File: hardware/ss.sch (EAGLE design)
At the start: 76 parts, among them IC1 DS3231, Q1 BSS138, Q3 si2305cd, Q4 si2305cd, Q5 8MHz, Q6 si2305cd, U1 SPX5205 3v3, U17 AVR_SPI_PRG_6PTH, U2 CN3083, U3 SPX5205 3v3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

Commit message: latest
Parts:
- removed BAT1: 3v, SparkFun:BATTERY12MM
- removed Q3: si2305cd, Simplex-DiscreteSemi:MOSFET-PCHANNELSMD_POWER
- added C22: 100nF, rcl:C-EUC0805
- added JP11: analog, SparkFun:M06SIP
- added JP14: digital, SparkFun-Connectors:M07
- added JP8: JUMPER-3SMD, SparkFun-Passives:JUMPER-3SMD
- added JP9: Kterm, SparkFun:M02PTH
- added Q2: si2305cd, Simplex-DiscreteSemi:MOSFET-PCHANNELSMD_POWER
- added R16: 100k, rcl:R-EU_R0805W
- added SJ3, SJ4: SOLDERJUMPERTRACE, SparkFun-Passives:SOLDERJUMPERTRACE
- added T1: BC846, transistor:BC846
- added U$3: MAX6675, SparkFun-AnalogIC:MAX6675
- JP4: value uC -> M01PTH; device SparkFun:M02PTH -> SparkFun-Connectors:M01PTH
- JP5: value digital -> 3v Li bat; device SparkFun-Connectors:M081X08 -> SparkFun:M02PTH
- JP6: value analog -> rxtx; device SparkFun-Connectors:M06SIP -> SparkFun:M02PTH
- LED1: value red -> charging; device SparkFun:LED0603 -> led:LEDCHIP-LED0805
- LED2: value green -> full; device SparkFun:LED0603 -> led:LEDCHIP-LED0805
- LED4: device SparkFun:LED0603 -> led:LEDCHIP-LED0805
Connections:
- removed net D4: JP5.2, U5.PD4(XCK/T0)
- removed net N$4: IC1.SDA, JP4.2, R13.2
- removed net N$6: IC1.SCL, JP4.1, R10.2
- removed net XBEE_IN: C18.1, C20.1, Q3.D, U3.EN, U3.IN
- removed net XBEE_PWR_SW: Q3.G, R1.2, U$2.DTR, U5.PC2(ADC2)
- new net A2: JP8.2, JP8.3, U5.PC2(ADC2)
- new net A3: JP11.4, U5.PC3(ADC3)
- new net N$100: C16.1, C17.1, Q2.S, R1.2, SJ3.2, U3.OUT
- new net N$26: R7.1, T1.B
- new net N$27: Q4.G, R16.2, T1.C
- new net N$29: JP9.1, U$3.T+
- new net N$30: JP9.2, U$3.T-
- new net XBEE_HIB: SJ4.1, U$2.DTR
- new net XBEE_PWR_SW_M: JP8.1, Q2.G, R1.1
- net +3V3: now also C22.1, U$3.VDD
- net +3V3_XBEE: now also Q2.D, SJ3.1; no longer C16.1, C17.1, U3.OUT
- net A0: now also JP11.2; no longer JP6.1
- net A1: now also JP11.3; no longer JP6.2
- net A6: now also JP4.1; no longer JP6.5
- net A7: now also JP11.1; no longer JP6.6
- net BOOST_SW: now also U5.PD4(XCK/T0); no longer Q4.G, U5.PC3(ADC3)
- net D3: now also JP14.2; no longer JP5.1
- net D5: now also JP14.3; no longer JP5.3
- net D6: now also JP14.4; no longer JP5.4
- net D7: now also JP14.5; no longer JP5.5
- net D8: now also JP14.6; no longer JP5.6
- net D9: now also JP14.7, U$3.CS; no longer JP5.7
- net GND: now also C22.2, JP5.2, SJ4.2, T1.E, U$3.VSS; no longer BAT1.-
- net H1: now also JP14.1; no longer JP5.8
- net MISO: now also U$3.MISO
- net N$10: now also JP5.1; no longer BAT1.+
- net RXI: now also JP6.1
- net SCK: now also U$3.SCK
- net SCL: now also IC1.SCL, JP11.6, R10.2; no longer JP6.4
- net SDA: now also IC1.SDA, JP11.5, R13.2; no longer JP6.3
- net TXO: now also JP6.2
- net V+: no longer Q3.S, Q4.S, R1.1, R7.1
- net VIN: now also C18.1, C20.1, Q4.S, R16.1, U3.EN, U3.IN
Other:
- moved on the sheet: C16, C17, C18, C19, C20, LED1, LED2, LED4, Q4, R1, R7, U3

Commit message: latest
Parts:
- removed JP8: JUMPER-3SMD, SparkFun-Passives:JUMPER-3SMD
- removed SJ3, SJ4: SOLDERJUMPERTRACE, SparkFun-Passives:SOLDERJUMPERTRACE
- added JP10: power, SparkFun:M02PTH
- added SJ345: J345, Simplex-Jumpers:SJ_4P
- added SJ6: J6, jumper:SJ
- JP4: value M01PTH -> a6
- SJ1: value SOLDERJUMPERTRACE -> J1; device SparkFun-Passives:SOLDERJUMPERTRACE -> jumper:SJ
- SJ2: value SOLDERJUMPERTRACE -> J2; device SparkFun-Passives:SOLDERJUMPERTRACE -> jumper:SJ
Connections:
- removed net A2: JP8.2, JP8.3, U5.PC2(ADC2)
- removed net N$100: C16.1, C17.1, Q2.S, R1.2, SJ3.2, U3.OUT
- removed net N$18: SJ2.2, U$2.RSSI
- removed net N$20: R8.2, SJ2.1
- new net N$7: R8.2, SJ6.1, SJ6.2, U$2.RSSI
- net +3V3_XBEE: now also C16.1, C17.1, Q2.S, R1.2, SJ2.1, SJ2.2, U3.OUT; no longer SJ3.1
- net GND: now also JP10.1, SJ345.4; no longer SJ4.2
- net N$12: now also JP10.2
- net XBEE_HIB: now also SJ345.2, SJ345.3, U5.PC2(ADC2); no longer SJ4.1
- net XBEE_PWR_SW_M: now also SJ345.1; no longer JP8.1
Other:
- note added: "J1 set - enable RST after schetch upload via xbee (default OPEN)"
- note added: "J2 set - xbee always has power on Vdd (default SET)"
- note added: "J3 set - xbee power controlled by external mosfet (default OPEN)"
- note added: "J4 set - xbee power controlled by ATSM1 (pin wake mode) (default SET)"
- note added: "J5 set - xbee always up if ATSM1 (pin wake mode) is used (default OPEN)"
- note added: "J6 set - xbee RSSI (Receive Signal Strength Indicator) displayed via an LED (default SET)"
- note added: "solder jumper settings"
- note added: "some combinations of J2,3,4,5 can fry devices. think twice."
- moved on the sheet: JP11, JP4

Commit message: latest
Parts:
- removed X1: USBSMD, SparkFun-Connectors:USBSMD
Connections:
- removed net N$23: LED4.A, R8.1
- new net N$6: LED4.C, R8.2
- net GND: now also R8.1, SJ6.1, SJ6.2; no longer LED4.C, X1.GND
- net N$12: no longer X1.VBUS
- net N$7: now also LED4.A; no longer R8.2, SJ6.1, SJ6.2
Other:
- moved on the sheet: JP10, JP2, LED4, SJ6
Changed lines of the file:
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@@
 <part name="GND7" library="SparkFun" deviceset="GND" device=""/>
 <part name="GND8" library="SparkFun" deviceset="GND" device=""/>
-<part name="GND12" library="SparkFun" deviceset="GND" device=""/>
 <part name="R5" library="rcl" deviceset="R-EU_" device="R0805W" value="1K"/>
 <part name="C5" library="rcl" deviceset="C-EU" device="C1206" value="10uF"/>
@@
 <part name="C20" library="rcl" deviceset="C-EU" device="C0805" value="100nF"/>
 <part name="GND32" library="SparkFun" deviceset="GND" device=""/>
-<part name="X1" library="SparkFun-Connectors" deviceset="USB" device="SMD"/>
 <part name="C15" library="rcl" deviceset="C-EU" device="C0805" value="100nF"/>
 <part name="Q4" library="Simplex-DiscreteSemi" deviceset="MOSFET-PCHANNEL" device="SMD_POWER" value="si2305cd"/>
@@
 <instance part="GND7" gate="1" x="33.02" y="149.86"/>
 <instance part="GND8" gate="1" x="48.26" y="149.86"/>
-<instance part="GND12" gate="1" x="15.24" y="149.86"/>
 <instance part="R5" gate="G$1" x="35.56" y="182.88" rot="R180"/>
 <instance part="C5" gate="G$1" x="78.74" y="160.02"/>
@@
 <instance part="IC1" gate="G$1" x="182.88" y="25.4"/>
 <instance part="GND21" gate="1" x="165.1" y="5.08"/>
-<instance part="JP2" gate="G$1" x="17.78" y="121.92" rot="R90"/>
+<instance part="JP2" gate="G$1" x="7.62" y="132.08"/>
 <instance part="+3V1" gate="G$1" x="86.36" y="139.7"/>
 <instance part="+3V2" gate="G$1" x="152.4" y="43.18"/>
@@
 <instance part="+3V6" gate="G$1" x="228.6" y="55.88"/>
 <instance part="P+4" gate="1" x="88.9" y="175.26"/>
-<instance part="P+5" gate="1" x="15.24" y="139.7"/>
+<instance part="P+5" gate="1" x="20.32" y="139.7"/>
 <instance part="P+6" gate="1" x="132.08" y="43.18"/>
 <instance part="P+9" gate="1" x="10.16" y="38.1"/>
@@
 <instance part="C20" gate="G$1" x="15.24" y="86.36"/>
 <instance part="GND32" gate="1" x="15.24" y="76.2"/>
-<instance part="X1" gate="G$1" x="10.16" y="162.56" rot="MR0"/>
 <instance part="C15" gate="G$1" x="20.32" y="160.02"/>
 <instance part="Q4" gate="G$1" x="10.16" y="60.96" rot="MR180"/>
@@
 <instance part="GND43" gate="1" x="203.2" y="190.5"/>
 <instance part="JP9" gate="G$1" x="205.74" y="210.82" rot="R180"/>
-<instance part="LED4" gate="G$1" x="254" y="167.64" rot="MR90"/>
+<instance part="LED4" gate="G$1" x="274.32" y="167.64" rot="MR90"/>
 <instance part="JP5" gate="G$1" x="223.52" y="20.32" rot="R180"/>
 <instance part="LED2" gate="G$1" x="55.88" y="187.96" rot="MR270"/>
@@
 <instance part="JP4" gate="G$1" x="287.02" y="91.44" rot="R180"/>
 <instance part="JP14" gate="G$1" x="304.8" y="83.82" rot="R180"/>
-<instance part="JP10" gate="G$1" x="7.62" y="177.8"/>
-<instance part="GND46" gate="1" x="15.24" y="172.72"/>
+<instance part="JP10" gate="G$1" x="7.62" y="162.56"/>
+<instance part="GND46" gate="1" x="15.24" y="149.86"/>
 <instance part="SJ1" gate="1" x="325.12" y="172.72"/>
-<instance part="SJ6" gate="1" x="274.32" y="167.64"/>
+<instance part="SJ6" gate="1" x="254" y="167.64"/>
 <instance part="SJ2" gate="1" x="93.98" y="88.9" rot="R90"/>
 <instance part="SJ345" gate="G$1" x="241.3" y="129.54"/>
@@
 </segment>
 <segment>
-<wire x1="12.7" y1="162.56" x2="15.24" y2="162.56" width="0.1524" layer="91"/>
-<wire x1="15.24" y1="162.56" x2="15.24" y2="152.4" width="0.1524" layer="91"/>
-<pinref part="GND12" gate="1" pin="GND"/>
-<pinref part="X1" gate="G$1" pin="GND"/>
-</segment>
-<segment>
 <wire x1="35.56" y1="170.18" x2="33.02" y2="170.18" width="0.1524" layer="91"/>
 <wire x1="33.02" y1="170.18" x2="33.02" y2="152.4" width="0.1524" layer="91"/>
@@
 </segment>
 <segment>
-<pinref part="GND34" gate="1" pin="GND"/>
-<wire x1="248.92" y1="162.56" x2="248.92" y2="167.64" width="0.1524" layer="91"/>
-<pinref part="LED4" gate="G$1" pin="C"/>
-</segment>
-<segment>
 <pinref part="T1" gate="G$1" pin="E"/>
 <pinref part="GND33" gate="1" pin="GND"/>
@@
 <pinref part="JP10" gate="G$1" pin="1"/>
 <pinref part="GND46" gate="1" pin="GND"/>
-<wire x1="15.24" y1="177.8" x2="15.24" y2="175.26" width="0.1524" layer="91"/>
+<wire x1="15.24" y1="162.56" x2="15.24" y2="152.4" width="0.1524" layer="91"/>
 </segment>
 <segment>
@@
 <wire x1="228.6" y1="129.54" x2="236.22" y2="129.54" width="0.1524" layer="91"/>
 </segment>
+<segment>
+<pinref part="GND34" gate="1" pin="GND"/>
+<pinref part="SJ6" gate="1" pin="1"/>
+<wire x1="248.92" y1="162.56" x2="248.92" y2="167.64" width="0.1524" layer="91"/>
+<wire x1="248.92" y1="167.64" x2="248.92" y2="172.72" width="0.1524" layer="91"/>
+<wire x1="248.92" y1="172.72" x2="259.08" y2="172.72" width="0.1524" layer="91"/>
+<pinref part="R8" gate="G$1" pin="1"/>
+<pinref part="SJ6" gate="1" pin="2"/>
+<wire x1="259.08" y1="172.72" x2="259.08" y2="167.64" width="0.1524" layer="91"/>
+<junction x="248.92" y="167.64"/>
+<junction x="259.08" y="167.64"/>
+</segment>
 </net>
 <net name="VIN" class="0">
@@
 <wire x1="40.64" y1="132.08" x2="40.64" y2="121.92" width="0.1524" layer="91"/>
 <wire x1="40.64" y1="121.92" x2="50.8" y2="121.92" width="0.1524" layer="91"/>
-<wire x1="17.78" y1="129.54" x2="17.78" y2="132.08" width="0.1524" layer="91"/>
-<wire x1="17.78" y1="132.08" x2="27.94" y2="132.08" width="0.1524" layer="91"/>
+<wire x1="15.24" y1="132.08" x2="27.94" y2="132.08" width="0.1524" layer="91"/>
 <wire x1="27.94" y1="132.08" x2="35.56" y2="132.08" width="0.1524" layer="91"/>
 <wire x1="35.56" y1="132.08" x2="40.64" y2="132.08" width="0.1524" layer="91"/>
@@
 <wire x1="30.48" y1="182.88" x2="27.94" y2="182.88" width="0.1524" layer="91"/>
 <wire x1="27.94" y1="182.88" x2="27.94" y2="165.1" width="0.1524" layer="91"/>
-<wire x1="12.7" y1="165.1" x2="20.32" y2="165.1" width="0.1524" layer="91"/>
 <wire x1="20.32" y1="165.1" x2="27.94" y2="165.1" width="0.1524" layer="91"/>
 <wire x1="27.94" y1="165.1" x2="27.94" y2="162.56" width="0.1524" layer="91"/>
@@
 <pinref part="R5" gate="G$1" pin="2"/>
 <pinref part="C14" gate="G$1" pin="+"/>
-<pinref part="X1" gate="G$1" pin="VBUS"/>
 <pinref part="C15" gate="G$1" pin="1"/>
 <pinref part="JP10" gate="G$1" pin="2"/>
-<wire x1="15.24" y1="180.34" x2="20.32" y2="180.34" width="0.1524" layer="91"/>
-<wire x1="20.32" y1="180.34" x2="20.32" y2="165.1" width="0.1524" layer="91"/>
+<wire x1="15.24" y1="165.1" x2="20.32" y2="165.1" width="0.1524" layer="91"/>
 </segment>
 </net>
@@
 </segment>
 <segment>
-<wire x1="15.24" y1="137.16" x2="15.24" y2="129.54" width="0.1524" layer="91"/>
-<pinref part="P+5" gate="1" pin="V+"/>
-<pinref part="JP2" gate="G$1" pin="2"/>
-</segment>
-<segment>
 <wire x1="132.08" y1="40.64" x2="132.08" y2="30.48" width="0.1524" layer="91"/>
 <wire x1="132.08" y1="30.48" x2="134.62" y2="30.48" width="0.1524" layer="91"/>
@@
 <pinref part="R11" gate="G$1" pin="2"/>
 <pinref part="Q6" gate="G$1" pin="S"/>
+</segment>
+<segment>
+<pinref part="JP2" gate="G$1" pin="2"/>
+<pinref part="P+5" gate="1" pin="V+"/>
+<wire x1="15.24" y1="134.62" x2="20.32" y2="134.62" width="0.1524" layer="91"/>
+<wire x1="20.32" y1="134.62" x2="20.32" y2="137.16" width="0.1524" layer="91"/>
 </segment>
 </net>
@@
 </segment>
 </net>
-<net name="N$23" class="0">
-<segment>
-<pinref part="R8" gate="G$1" pin="1"/>
-<pinref part="LED4" gate="G$1" pin="A"/>
-<wire x1="256.54" y1="167.64" x2="259.08" y2="167.64" width="0.1524" layer="91"/>
-</segment>
-</net>
 <net name="A6" class="0">
 <segment>
@@
 </segment>
 </net>
+<net name="N$6" class="0">
+<segment>
+<pinref part="R8" gate="G$1" pin="2"/>
+<pinref part="LED4" gate="G$1" pin="C"/>
+</segment>
+</net>
 <net name="N$7" class="0">
 <segment>
-<pinref part="R8" gate="G$1" pin="2"/>
-<pinref part="SJ6" gate="1" pin="1"/>
-<wire x1="269.24" y1="167.64" x2="269.24" y2="170.18" width="0.1524" layer="91"/>
-<wire x1="269.24" y1="170.18" x2="276.86" y2="170.18" width="0.1524" layer="91"/>
-<wire x1="276.86" y1="170.18" x2="276.86" y2="167.64" width="0.1524" layer="91"/>
+<pinref part="LED4" gate="G$1" pin="A"/>
 <pinref part="U$2" gate="G$1" pin="RSSI"/>
-<pinref part="SJ6" gate="1" pin="2"/>
 <wire x1="276.86" y1="167.64" x2="279.4" y2="167.64" width="0.1524" layer="91"/>
-<junction x="269.24" y="167.64"/>
-<junction x="279.4" y="167.64"/>
-</segment>
-</net>
+</segment>
+</net>

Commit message: hopefully flawless
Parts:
- removed Q2: si2305cd, Simplex-DiscreteSemi:MOSFET-PCHANNELSMD_POWER
- removed R1: 100k, rcl:R-EU_R0805W
- added Q3: si2305cd, Simplex-DiscreteSemi:MOSFET-PCHANNELSMD_POWER
- added R17: 1M, rcl:R-EU_R0805W
- added R18: 100k, rcl:R-EU_R0805W
- added T2: BC846, transistor:BC846
- R7: value 100k -> 1M
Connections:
- new net N$18: R17.1, T2.B
- new net N$20: Q3.G, R18.2, T2.C
- net +3V3_XBEE: no longer Q2.D, Q2.S, R1.2, SJ2.1, SJ2.2
- net GND: now also T2.E
- net VIN: now also Q3.D, Q3.S, R18.1, SJ2.1, SJ2.2
- net XBEE_PWR_SW_M: now also R17.2; no longer Q2.G, R1.1
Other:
- moved on the sheet: C1, C14, C15, C16, C17, C18, C19, C2, C20, C3, C4, C5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

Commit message: d9 needs external weak pullup during programming
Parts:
- added R1: 100K, rcl:R-EU_R0805W
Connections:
- net +3V3: now also R1.2
- net D9: now also R1.1
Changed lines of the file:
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@@
 <part name="R18" library="rcl" deviceset="R-EU_" device="R0805W" value="100k"/>
 <part name="SJ2" library="jumper" deviceset="SJ" device="" value="J2"/>
+<part name="+3V9" library="supply1" deviceset="+3V3" device=""/>
+<part name="R1" library="rcl" deviceset="R-EU_" device="R0805W" value="100K"/>
 </parts>
 <sheets>
@@
 <instance part="R18" gate="G$1" x="0" y="129.54" rot="R270"/>
 <instance part="SJ2" gate="1" x="30.48" y="127" rot="R90"/>
+<instance part="+3V9" gate="G$1" x="233.68" y="99.06"/>
+<instance part="R1" gate="G$1" x="223.52" y="91.44"/>
 </instances>
 <busses>
@@
 <junction x="149.86" y="210.82"/>
 </segment>
+<segment>
+<pinref part="+3V9" gate="G$1" pin="+3V3"/>
+<wire x1="233.68" y1="91.44" x2="233.68" y2="96.52" width="0.1524" layer="91"/>
+<pinref part="R1" gate="G$1" pin="2"/>
+<wire x1="228.6" y1="91.44" x2="233.68" y2="91.44" width="0.1524" layer="91"/>
+</segment>
 </net>
 <net name="+5V" class="0">
@@
 <segment>
 <pinref part="U5" gate="G$1" pin="PD4(XCK/T0)"/>
+<label x="210.82" y="106.68" size="1.778" layer="95"/>
 <wire x1="208.28" y1="106.68" x2="215.9" y2="106.68" width="0.1524" layer="91"/>
-<label x="210.82" y="106.68" size="1.778" layer="95"/>
 </segment>
 </net>
@@
 <segment>
 <pinref part="U5" gate="G$1" pin="PB1(OC1A)"/>
-<wire x1="208.28" y1="91.44" x2="215.9" y2="91.44" width="0.1524" layer="91"/>
+<wire x1="208.28" y1="91.44" x2="218.44" y2="91.44" width="0.1524" layer="91"/>
 <label x="210.82" y="91.44" size="1.778" layer="95"/>
-</segment>
-<segment>
+<pinref part="R1" gate="G$1" pin="1"/>
+</segment>
+<segment>

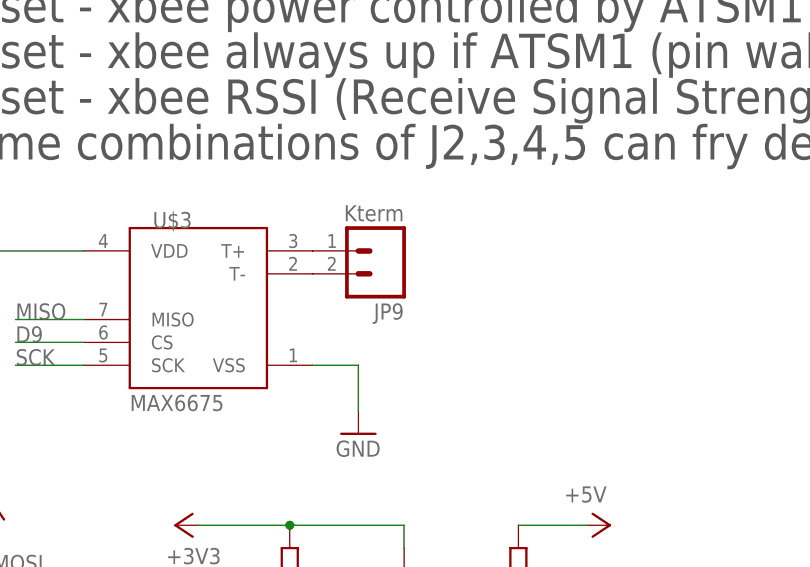
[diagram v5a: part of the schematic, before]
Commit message: thermocouple t- must be grounded
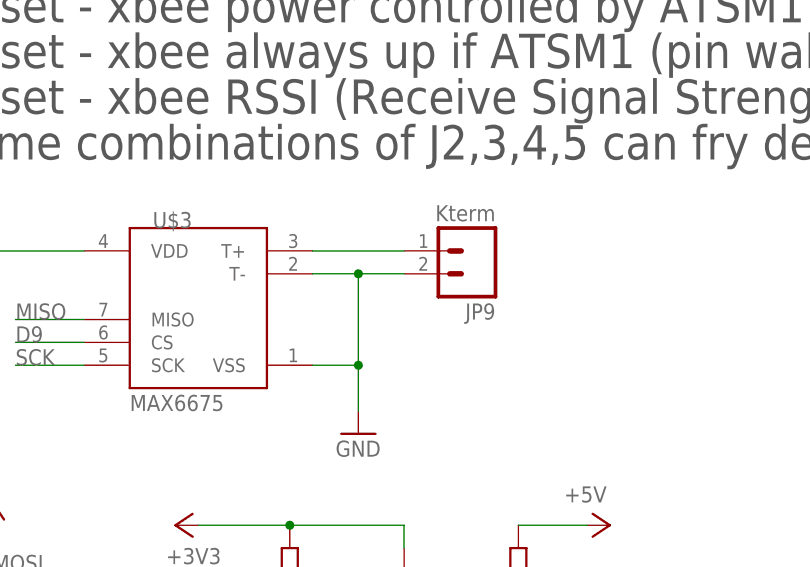
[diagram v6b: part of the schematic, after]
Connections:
- removed net N$30: JP9.2, U$3.T-
- net GND: now also JP9.2, U$3.T-
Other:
- moved on the sheet: JP9
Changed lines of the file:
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@@
 <instance part="GND37" gate="1" x="149.86" y="190.5"/>
 <instance part="GND43" gate="1" x="203.2" y="190.5"/>
-<instance part="JP9" gate="G$1" x="205.74" y="210.82" rot="R180"/>
+<instance part="JP9" gate="G$1" x="215.9" y="210.82" rot="R180"/>
 <instance part="LED4" gate="G$1" x="274.32" y="167.64" rot="MR90"/>
 <instance part="JP5" gate="G$1" x="223.52" y="20.32" rot="R180"/>
@@
 <wire x1="198.12" y1="198.12" x2="203.2" y2="198.12" width="0.1524" layer="91"/>
 <wire x1="203.2" y1="198.12" x2="203.2" y2="193.04" width="0.1524" layer="91"/>
+<pinref part="U$3" gate="G$1" pin="T-"/>
+<pinref part="JP9" gate="G$1" pin="2"/>
+<wire x1="208.28" y1="208.28" x2="203.2" y2="208.28" width="0.1524" layer="91"/>
+<wire x1="203.2" y1="208.28" x2="198.12" y2="208.28" width="0.1524" layer="91"/>
+<wire x1="203.2" y1="198.12" x2="203.2" y2="208.28" width="0.1524" layer="91"/>
+<junction x="203.2" y="198.12"/>
+<junction x="203.2" y="208.28"/>
 </segment>
 <segment>
@@
 <pinref part="U$3" gate="G$1" pin="T+"/>
 <pinref part="JP9" gate="G$1" pin="1"/>
-</segment>
-</net>
-<net name="N$30" class="0">
-<segment>
-<pinref part="U$3" gate="G$1" pin="T-"/>
-<pinref part="JP9" gate="G$1" pin="2"/>
-</segment>
-</net>
+<wire x1="208.28" y1="210.82" x2="198.12" y2="210.82" width="0.1524" layer="91"/>
+</segment>
+</net>

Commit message: move power socket
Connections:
- net N$29 renamed T+
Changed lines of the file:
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@@
 </segment>
 </net>
-<net name="N$29" class="0">
+<net name="T+" class="0">
 <segment>
 <pinref part="U$3" gate="G$1" pin="T+"/>
